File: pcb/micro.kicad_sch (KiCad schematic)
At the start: 25 parts, among them SW1 BOOT, SW2 RST, U1 RP2040, U5 W25Q128JVSIQ, Y1 12MHz

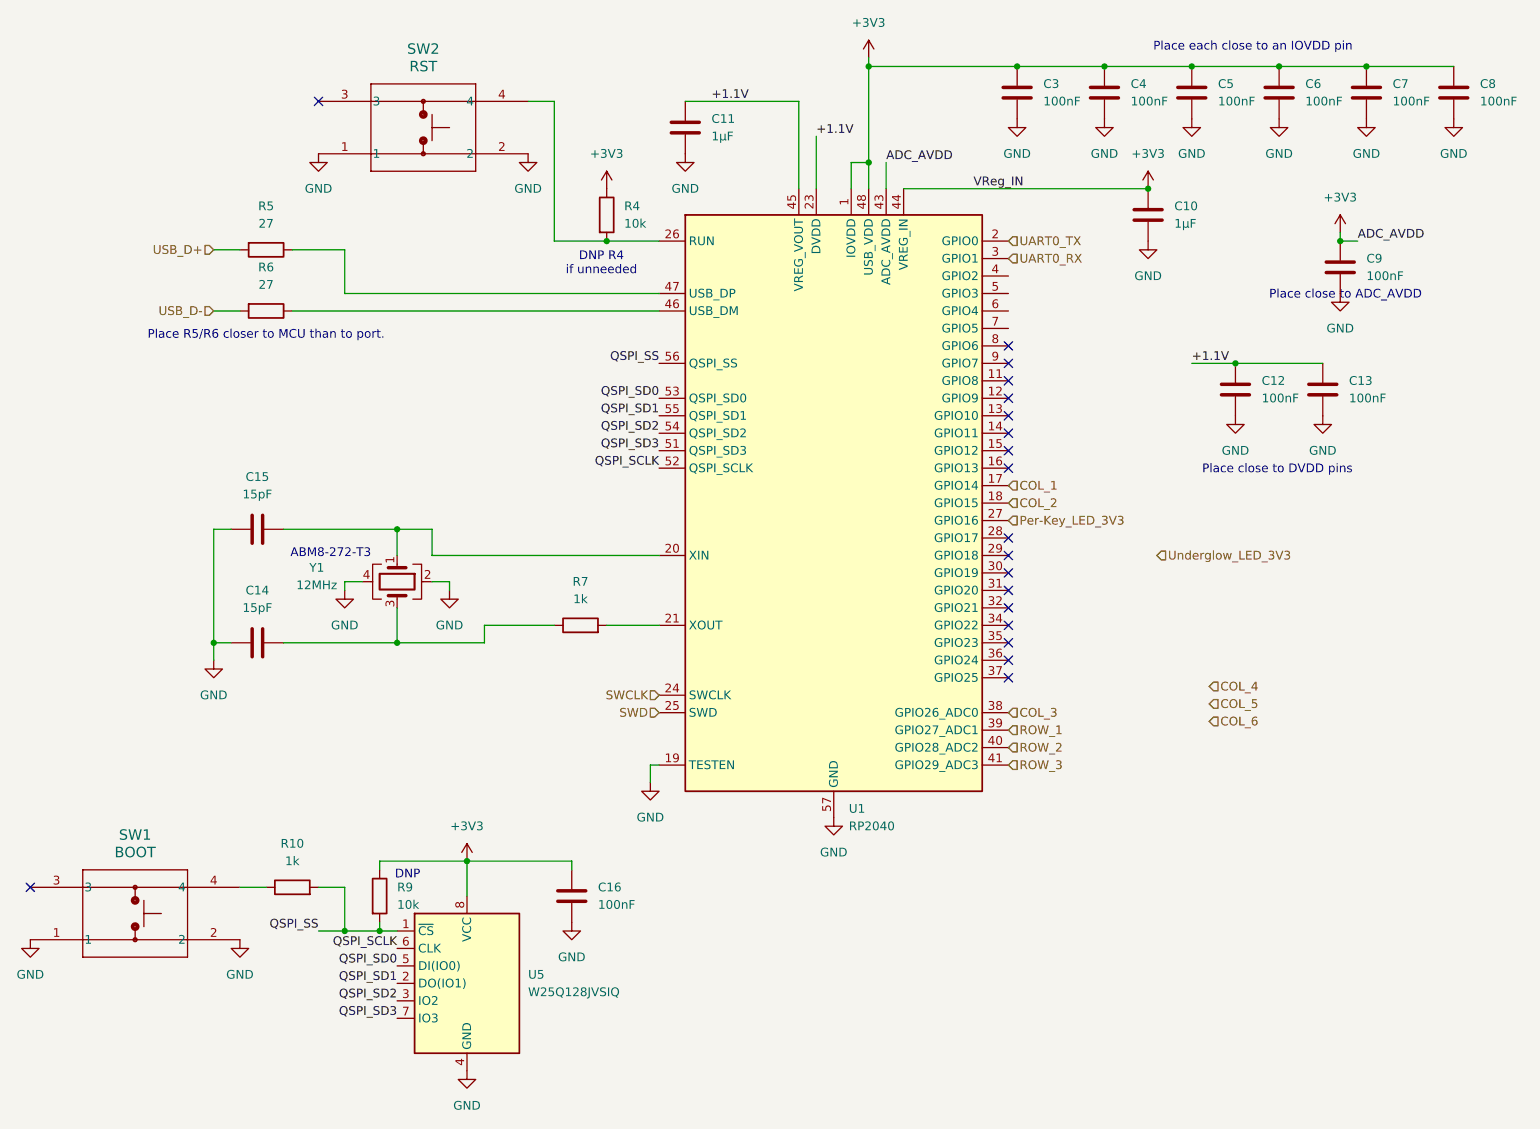
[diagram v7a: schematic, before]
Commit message: Adding reversible MX Sockets and SK6812MiniE footprints, finishing the replacement of Ethernet with a TRRS connector and selectable 0Ohm resistors to swap Rx/Tx for the interconnect.
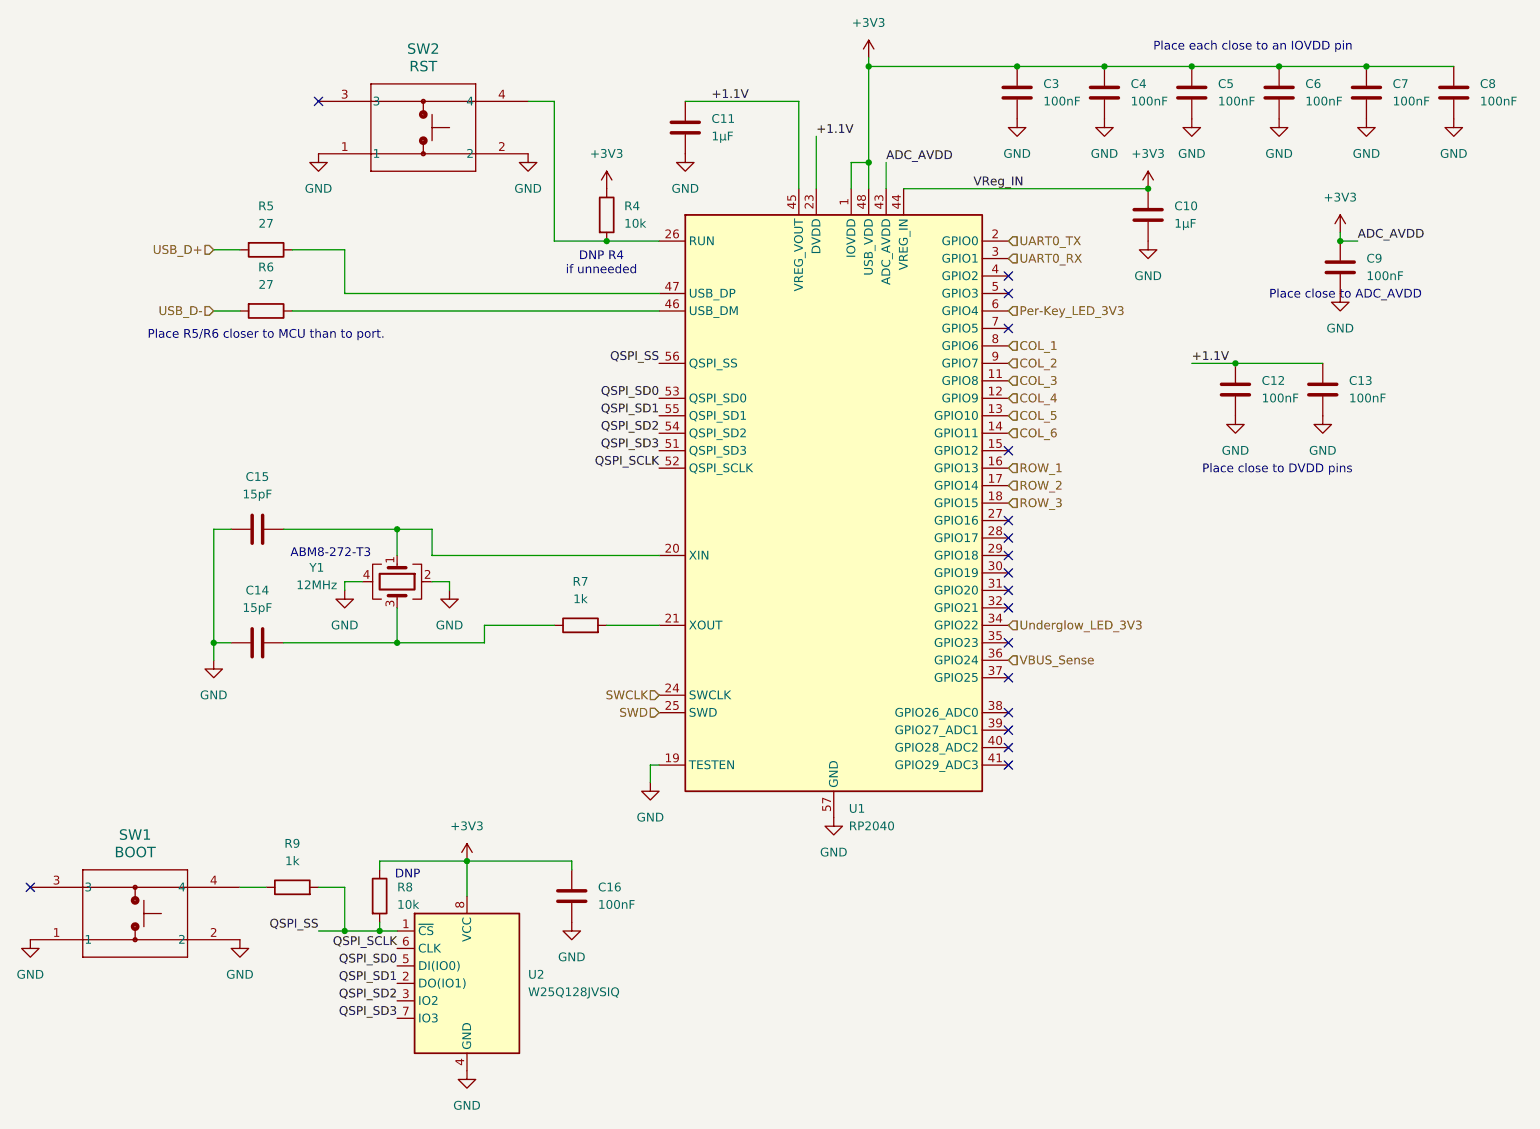
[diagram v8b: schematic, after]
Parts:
- renumbered R9 to R8, R10 to R9, U5 to U2
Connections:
- net COL_1: now also U1.8 (GPIO6); no longer U1.17 (GPIO14)
- net COL_2: now also U1.9 (GPIO7); no longer U1.18 (GPIO15)
- net COL_3: now also U1.11 (GPIO8); no longer U1.38 (GPIO26_ADC0)
- net COL_4: now also U1.12 (GPIO9)
- net COL_5: now also U1.13 (GPIO10)
- net COL_6: now also U1.14 (GPIO11)
- net Per-Key_LED_3V3: now also U1.6 (GPIO4); no longer U1.27 (GPIO16)
- net ROW_1: now also U1.16 (GPIO13); no longer U1.39 (GPIO27_ADC1)
- net ROW_2: now also U1.17 (GPIO14); no longer U1.40 (GPIO28_ADC2)
- net ROW_3: now also U1.18 (GPIO15); no longer U1.41 (GPIO29_ADC3)
- net Underglow_LED_3V3: now also U1.34 (GPIO22)
- net VBUS_Sense: now reaches U1.36 (GPIO24)
- no-connect marks 19 -> 18
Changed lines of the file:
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@@
 	)
 	(no_connect
-		(at 177.8 115.57)
-	)
-	(no_connect
 		(at 177.8 102.87)
 	)
 	(no_connect
-		(at 177.8 74.93)
+		(at 177.8 100.33)
 	)
 	(no_connect
-		(at 177.8 100.33)
+		(at 177.8 95.25)
 	)
 	(no_connect
-		(at 177.8 82.55)
+		(at 177.8 67.31)
 	)
 	(no_connect
-		(at 177.8 80.01)
+		(at 177.8 123.19)
 	)
 	(no_connect
-		(at 177.8 69.85)
+		(at 177.8 125.73)
 	)
 	(no_connect
-		(at 177.8 87.63)
+		(at 177.8 130.81)
 	)
 	(no_connect
@@
 	)
 	(no_connect
-		(at 77.47 34.29)
+		(at 177.8 128.27)
 	)
 	(no_connect
-		(at 177.8 77.47)
+		(at 77.47 34.29)
 	)
 	(no_connect
@@
 	)
 	(no_connect
-		(at 177.8 85.09)
+		(at 177.8 62.23)
 	)
 	(no_connect
@@
 	)
 	(no_connect
-		(at 177.8 105.41)
+		(at 177.8 59.69)
 	)
 	(no_connect
-		(at 177.8 110.49)
+		(at 177.8 105.41)
 	)
 	(no_connect
-		(at 177.8 107.95)
+		(at 177.8 85.09)
 	)
 	(no_connect
-		(at 177.8 72.39)
+		(at 177.8 107.95)
 	)
 	(wire
@@
 	(hierarchical_label "ROW_1"
 		(shape input)
-		(at 177.8 125.73 0)
+		(at 177.8 87.63 0)
 		(fields_autoplaced yes)
 		(effects
@@
 	(hierarchical_label "COL_1"
 		(shape input)
-		(at 177.8 90.17 0)
+		(at 177.8 69.85 0)
 		(fields_autoplaced yes)
 		(effects
@@
 		)
 	)
+	(hierarchical_label "VBUS_Sense"
+		(shape input)
+		(at 177.8 115.57 0)
+		(fields_autoplaced yes)
+		(effects
+			(font
+				(size 1.27 1.27)
+			)
+			(justify left)
+		)
+	)
 	(hierarchical_label "UART0_RX"
 		(shape input)
@@
 	(hierarchical_label "COL_4"
 		(shape input)
-		(at 207.01 119.38 0)
+		(at 177.8 77.47 0)
 		(fields_autoplaced yes)
 		(effects
@@
 	(hierarchical_label "ROW_2"
 		(shape input)
-		(at 177.8 128.27 0)
+		(at 177.8 90.17 0)
 		(fields_autoplaced yes)
 		(effects
@@
 	(hierarchical_label "ROW_3"
 		(shape input)
-		(at 177.8 130.81 0)
+		(at 177.8 92.71 0)
 		(fields_autoplaced yes)
 		(effects
@@
 	(hierarchical_label "COL_5"
 		(shape input)
-		(at 207.01 121.92 0)
+		(at 177.8 80.01 0)
 		(fields_autoplaced yes)
 		(effects
@@
 	(hierarchical_label "COL_3"
 		(shape input)
-		(at 177.8 123.19 0)
+		(at 177.8 74.93 0)
 		(fields_autoplaced yes)
 		(effects
@@
 	(hierarchical_label "COL_2"
 		(shape input)
-		(at 177.8 92.71 0)
+		(at 177.8 72.39 0)
 		(fields_autoplaced yes)
 		(effects
@@
 	(hierarchical_label "Underglow_LED_3V3"
 		(shape input)
-		(at 199.39 100.33 0)
+		(at 177.8 110.49 0)
 		(fields_autoplaced yes)
 		(effects
@@
 	(hierarchical_label "COL_6"
 		(shape input)
-		(at 207.01 124.46 0)
+		(at 177.8 82.55 0)
 		(fields_autoplaced yes)
 		(effects
@@
 	(hierarchical_label "Per-Key_LED_3V3"
 		(shape input)
-		(at 177.8 95.25 0)
+		(at 177.8 64.77 0)
 		(fields_autoplaced yes)
 		(effects
@@
 		(on_board yes)
 		(dnp no)
-		(property "Reference" "U5"
+		(property "Reference" "U2"
 			(at 107.95 161.2899 0)
 			(effects
@@
 			(project ""
 				(path "/9203b006-47ac-4f34-8cc4-2b709e3df56f/b2f85b86-5933-4a5f-88c2-315afb4ca3cd"
-					(reference "U5")
+					(reference "U2")
 					(unit 1)
 				)
@@
 		(dnp no)
 		(fields_autoplaced yes)
-		(property "Reference" "R10"
+		(property "Reference" "R9"
 			(at 73.66 142.24 90)
 			(effects
@@
 			(project ""
 				(path "/9203b006-47ac-4f34-8cc4-2b709e3df56f/b2f85b86-5933-4a5f-88c2-315afb4ca3cd"
-					(reference "R10")
+					(reference "R9")
 					(unit 1)
 				)
@@
 		(dnp no)
 		(fields_autoplaced yes)
-		(property "Reference" "R9"
+		(property "Reference" "R8"
 			(at 88.9 148.5899 0)
 			(effects
@@
 			(project ""
 				(path "/9203b006-47ac-4f34-8cc4-2b709e3df56f/b2f85b86-5933-4a5f-88c2-315afb4ca3cd"
-					(reference "R9")
+					(reference "R8")
 					(unit 1)
 				)
